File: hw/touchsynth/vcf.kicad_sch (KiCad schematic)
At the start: 39 parts, among them Q4 BC847BS, Q5 BC847BS, Q6 BC847BS, Q7 BC847BS, Q8 BC847BS, Q9 BC847BS, U10 TL072, U12 LM324

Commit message: Schematic v2: hand-drawn sheet layouts with wires; MIDI in DNP
- draw.py/gen_sch2.py/layouts.py: placement + wiring per block, automatic
  labels for remaining split nets, short detection, junctions, KiCad
  endpoint-only connection semantics
- all 7 sheets laid out (ladder drawn as a transistor stack, diff amps,
  integrator with reset, R-2R DAC, ...); ERC 0 violations, netlist == design,
  145 simulated elements match
- MIDI input parts marked DNP (footprints kept)
- docs/touchsynth_schematic.pdf

Co-Authored-By: Claude Opus 5.5 (1M context) <noreply@anthropic.com>
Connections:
- net BIN1: no longer names the net of C35.2, Q5.2 (B1), R47.1
- net CVC_A: no longer names the net of C26.1, R41.2, R42.1
- net EXPO_E: no longer names the net of Q4.1 (E1), Q4.4 (E2), R46.2
- net EXPO_NA: no longer names the net of C29.2, Q4.6 (C1), R45.2, U12.9 (-)
- net EXPO_OUT: no longer names the net of C29.1, R46.1, U12.8
- net INA_A: no longer names the net of R49.1, R50.2, U10.2 (-)
- net INA_B: no longer names the net of R51.2, R52.2, U10.6 (-)
- net INA_OA: no longer names the net of R50.1, R51.1, U10.1
- net MIX: no longer names the net of C35.1, R53.2, R54.2, R55.2, R56.2, R57.1
- net N1A: no longer names the net of C30.1, Q5.6 (C1), Q6.1 (E1)
- net N1B: no longer names the net of C30.2, Q5.3 (C2), Q6.4 (E2)
- net N2A: no longer names the net of C31.1, Q6.6 (C1), Q7.1 (E1)
- net N2B: no longer names the net of C31.2, Q6.3 (C2), Q7.4 (E2)
- net N3A: no longer names the net of C32.1, Q7.6 (C1), Q8.1 (E1)
- net N3B: no longer names the net of C32.2, Q7.3 (C2), Q8.4 (E2)
- net XCUT: no longer names the net of C28.1, Q4.5 (B2), R43.2, R44.1
- net XCUT_IN: no longer names the net of C27.1, R42.2, R43.1, TP15.1
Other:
- note added: "CV_CUT: PWM filter and exponential converter (tail current of the ladder)"
- note added: "Output instrumentation amplifier across the top capacitor (G = 11, referenced to VREF)"
- note added: "Transistor ladder (4 poles, 4 x 33 nF), bias from VB0...VB4, mixer"
- note removed: "CV_CUT filter and exponential converter"
- note removed: "Mixer"
- note removed: "Output instrumentation amplifier (G = 11)"
- note removed: "Test points"
- note removed: "Transistor ladder (4 poles)"

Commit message: PCB placement by functional block, silkscreen art, discrete LED resistors
- gen_pcb.py / pcb_place.py: 100 x 100 mm 2-layer board; keys, LEDs, connectors and test points fixed,
  ICs anchored per block, remaining parts placed greedily by connectivity inside their block
- blocks tile the circuit area with a 0.35 mm street for the dashed silkscreen frames and a reserved
  title tab each (pcb_art.py); piano keybed with hatched black keys; logo, resonant saw and ladder
  response curves on the front; signal-flow diagram on the back
- LED resistor arrays replaced by 16 discrete 4.7k 0603 (basic part) next to each LED
- deterministic schematic UUIDs, net name labels for PCB parity, op-amp re-pairing, fab.py

Co-Authored-By: Claude Opus 5.5 (1M context) <noreply@anthropic.com>
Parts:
- removed R41, R46: 1k, Resistor_SMD:R_0603_1608Metric, symbol Device:R
- removed R42: 4.7k, Resistor_SMD:R_0603_1608Metric, symbol Device:R
- removed R43: 33k, Resistor_SMD:R_0603_1608Metric, symbol Device:R
- removed R44: 1.5k, Resistor_SMD:R_0603_1608Metric, symbol Device:R
- removed R45: 300k, Resistor_SMD:R_0603_1608Metric, symbol Device:R
- removed R47, R48, R50, R51: 10k, Resistor_SMD:R_0603_1608Metric, symbol Device:R
- removed R49, R52: 100k, Resistor_SMD:R_0603_1608Metric, symbol Device:R
- removed R53: 150k, Resistor_SMD:R_0603_1608Metric, symbol Device:R
- removed R54, R55, R56: 470k, Resistor_SMD:R_0603_1608Metric, symbol Device:R
- added R58: 4.7k, Resistor_SMD:R_0603_1608Metric, symbol Device:R
- added R59: 33k, Resistor_SMD:R_0603_1608Metric, symbol Device:R
- added R60: 1.5k, Resistor_SMD:R_0603_1608Metric, symbol Device:R
- added R61: 300k, Resistor_SMD:R_0603_1608Metric, symbol Device:R
- added R62: 1k, Resistor_SMD:R_0603_1608Metric, symbol Device:R
- added R63, R64, R66, R67, R73: 10k, Resistor_SMD:R_0603_1608Metric, symbol Device:R
- added R65, R68: 100k, Resistor_SMD:R_0603_1608Metric, symbol Device:R
- added R69: 150k, Resistor_SMD:R_0603_1608Metric, symbol Device:R
- added R70, R71, R72: 470k, Resistor_SMD:R_0603_1608Metric, symbol Device:R
- R57: value 10k -> 1k; LCSC C25804 -> C21190; Sim RMX -> R1C
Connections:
- net +5V: now also R61.1
- net BIN2: now also R64.1
- net LPF: now also R68.1
- net NOISE: now also R72.1
- net PULSE: now also R70.1
- net PWM_CUT: now also R57.1
- net SAW: now also R69.1
- net SUB: now also R71.1
- net VB0: now also R63.2, R64.2, R73.2; no longer R57.2
- net VBIAS: now also R60.2
- net VREF: now also R65.2
- net EXPO_OUT: now reaches C29.1, U12.8
- net EXPO_OUT: now also R62.1
- net EXPO_E: now reaches Q4.1 (E1), Q4.4 (E2)
- net EXPO_E: now also R62.2
- net XCUT_IN: now reaches C27.1, TP15.1
- net XCUT_IN: now also R58.2, R59.1
- net EXPO_NA: now reaches C29.2, Q4.6 (C1), U12.9 (-)
- net EXPO_NA: now also R61.2
- net XCUT: now reaches C28.1, Q4.5 (B2)
- net XCUT: now also R59.2, R60.1
- net INA_B: now reaches U10.6 (-)
- net INA_B: now also R67.2, R68.2
- net INA_OA: now reaches U10.1
- net INA_OA: now also R66.1, R67.1
- net INA_A: now reaches U10.2 (-)
- net INA_A: now also R65.1, R66.2
- net N1B: now reaches C30.2, Q5.3 (C2), Q6.4 (E2)
- net N3B: now reaches C32.2, Q7.3 (C2), Q8.4 (E2)
- net N3A: now reaches C32.1, Q7.6 (C1), Q8.1 (E1)
- net CVC_A: now reaches C26.1
- net CVC_A: now also R57.2, R58.1
- net MIX: now reaches C35.1
- net MIX: now also R69.2, R70.2, R71.2, R72.2, R73.1; no longer R57.1
- net BIN1: now reaches C35.2, Q5.2 (B1)
- net BIN1: now also R63.1
- net N2A: now reaches C31.1, Q6.6 (C1), Q7.1 (E1)
- net N2B: now reaches C31.2, Q6.3 (C2), Q7.4 (E2)
- net N1A: now reaches C30.1, Q5.6 (C1), Q6.1 (E1)

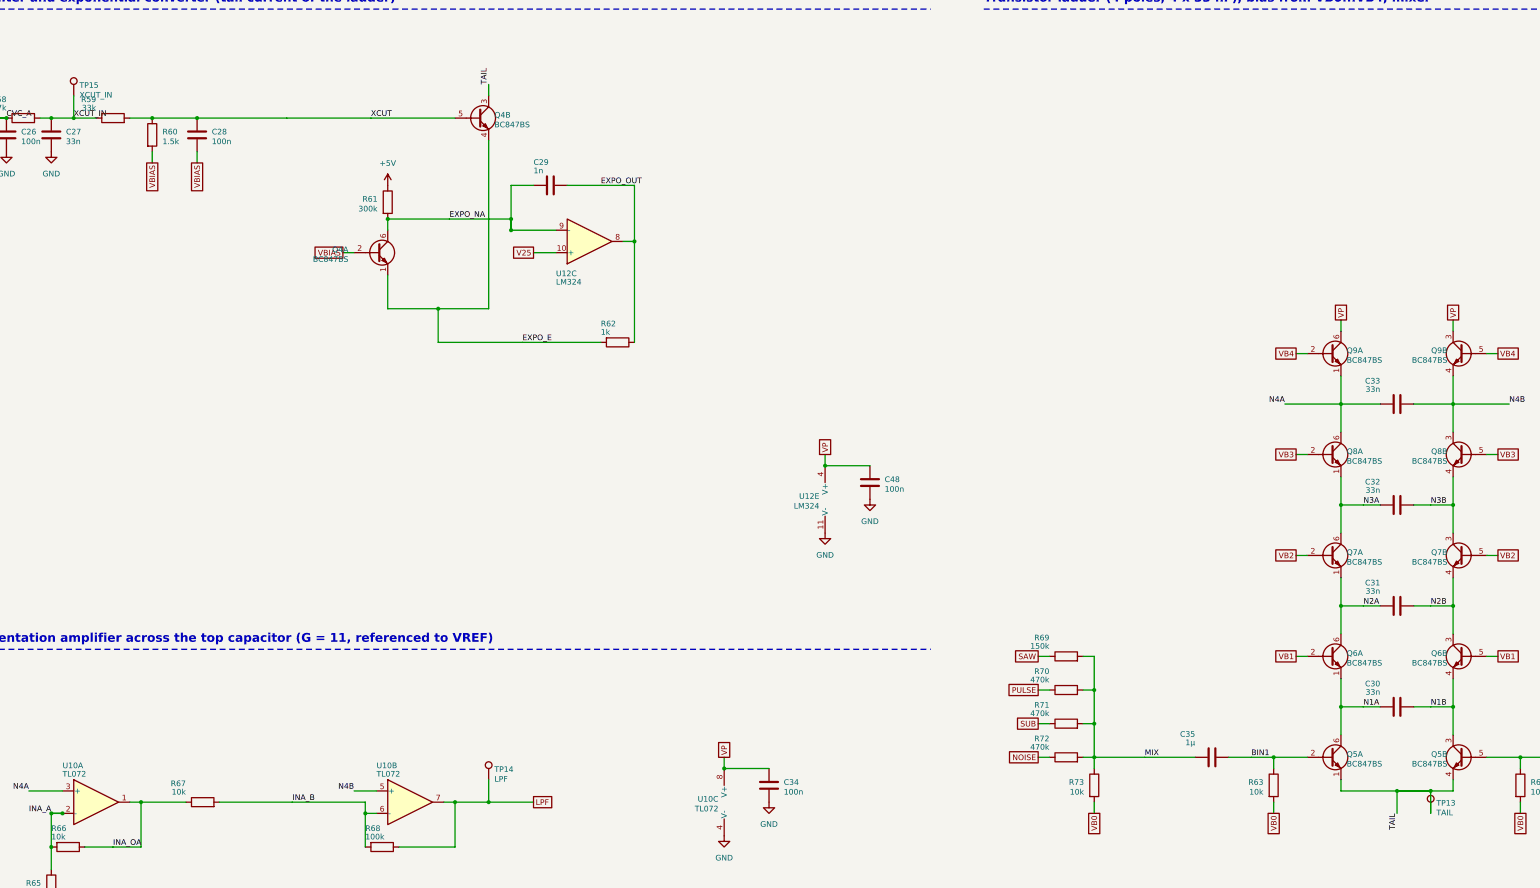
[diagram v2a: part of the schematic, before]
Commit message: 4-layer PCB: keys I/O row, trim DAC by the VCA, full routing and fab outputs
- 4 layers: F.Cu signals, In1 solid GND, In2 split power (VP analog / +5V digital / GND under the keys),
  B.Cu signals; no plane and no foreign tracks under the touch pads
- floorplan: analog blocks 72 x 36 mm in signal-flow order, right column MIDI / trim DAC / MCU,
  keys I/O row (touch muxes, LED shift registers) directly above the keys; shorter white keys,
  function pads flush with the keybed; test points inside their blocks, two THT scope-ground pins
- routing pipeline: plane stitch vias, pre-routed plane nets, Freerouting, GND via grid, island
  check, A* maze router for leftovers (pcb_maze.py), rip-up repair mode
- DRC: 0 violations, 0 unconnected, schematic parity OK; JLCPCB gerbers / BOM / CPL via fab.py
- silkscreen: back-side credits (design: cpldcpu & Claude Opus 5.5), vias kept out of the art

Co-Authored-By: Claude Opus 5.5 (1M context) <noreply@anthropic.com>
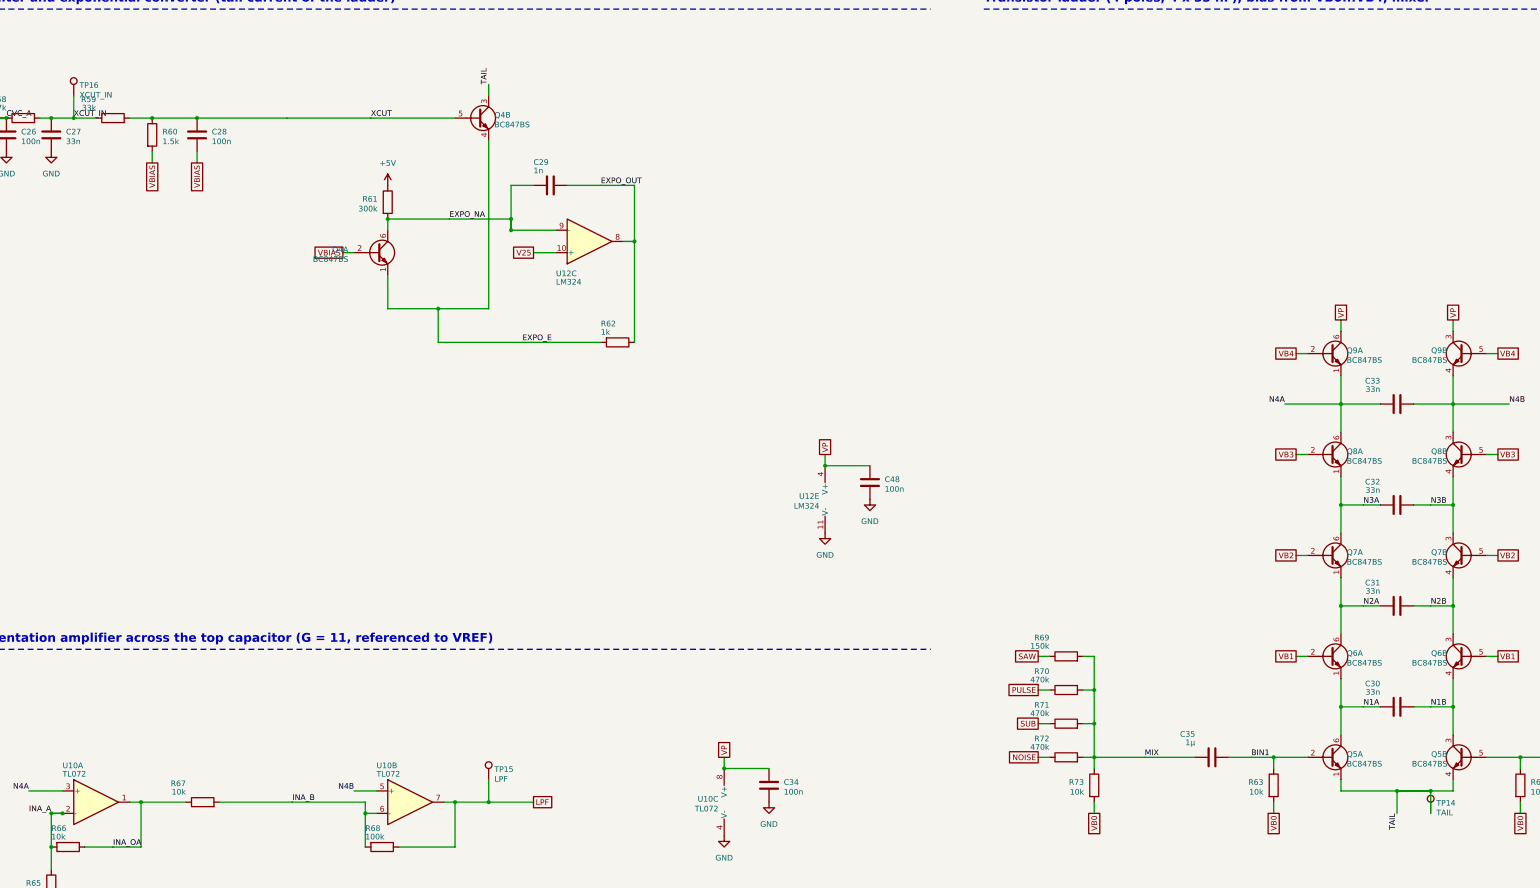
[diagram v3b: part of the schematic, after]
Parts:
- removed TP13: TAIL, TestPoint:TestPoint_Pad_D1.0mm, symbol Connector:TestPoint
- added TP16: XCUT_IN, TestPoint:TestPoint_Pad_D1.0mm, symbol Connector:TestPoint
- TP14: value LPF -> TAIL
- TP15: value XCUT_IN -> LPF
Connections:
- net LPF: now also TP15.1; no longer TP14.1
- net TAIL: now also TP14.1
- net XCUT_IN: now also TP16.1; no longer TP15.1
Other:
- moved on the sheet: TP14, TP15
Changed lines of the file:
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@@
 		(on_board yes)
 		(dnp no)
-		(property "Reference" "TP15"
+		(property "Reference" "TP16"
 			(at 57.18 48.449 0)
 			(effects
@@
 			(project "touchsynth"
 				(path "/c42cd0d4-93b1-5178-97ee-fdd3025be2c6/52d1c793-861a-5f85-89b7-e3423668fc78"
-					(reference "TP15")
+					(reference "TP16")
 					(unit 1)
 				)
@@
 		(on_board yes)
 		(dnp no)
-		(property "Reference" "TP13"
+		(property "Reference" "TP14"
 			(at 364.52 211.009 0)
 			(effects
@@
 			(project "touchsynth"
 				(path "/c42cd0d4-93b1-5178-97ee-fdd3025be2c6/52d1c793-861a-5f85-89b7-e3423668fc78"
-					(reference "TP13")
+					(reference "TP14")
 					(unit 1)
 				)
@@
 		(on_board yes)
 		(dnp no)
-		(property "Reference" "TP14"
+		(property "Reference" "TP15"
 			(at 151.16 203.389 0)
 			(effects
@@
 			(project "touchsynth"
 				(path "/c42cd0d4-93b1-5178-97ee-fdd3025be2c6/52d1c793-861a-5f85-89b7-e3423668fc78"
-					(reference "TP14")
+					(reference "TP15")
 					(unit 1)
 				)
